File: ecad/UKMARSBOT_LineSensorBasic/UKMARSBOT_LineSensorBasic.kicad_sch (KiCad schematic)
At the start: 32 parts, among them J1 Conn_01x16, Q1 BC337, Q2 BPW85C, Q3 BPW85C, Q4 BPW85C, Q5 BPW85C, Q6 BC337

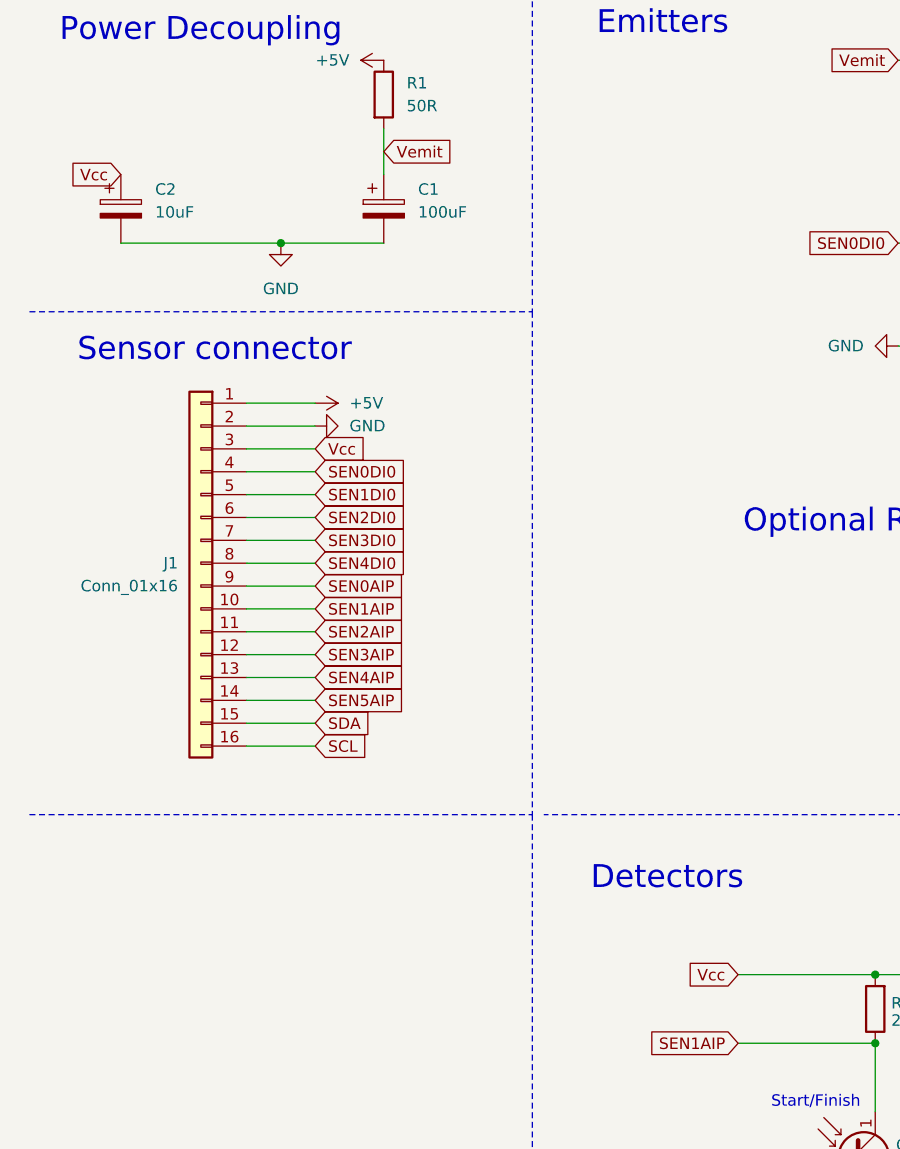
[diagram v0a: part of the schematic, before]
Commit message: Basic line sensor modified for new connector position
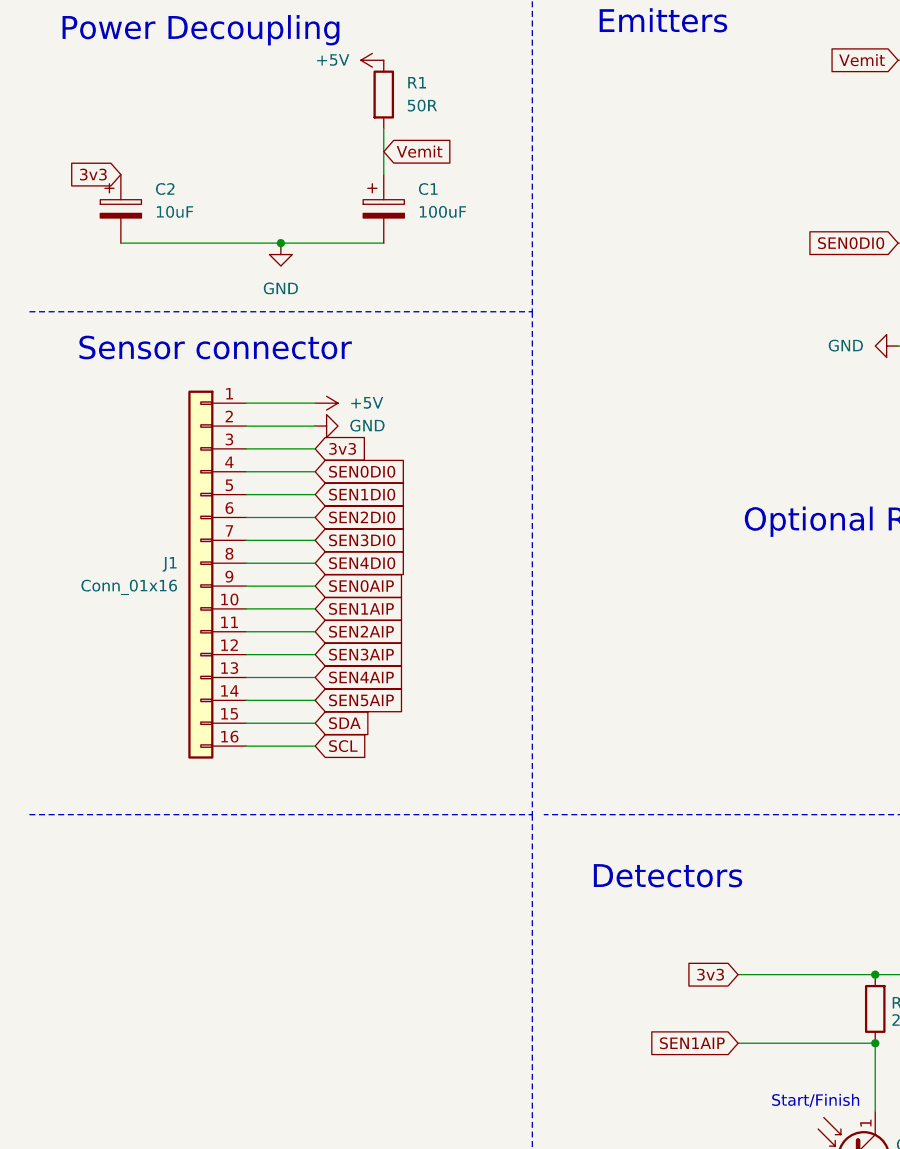
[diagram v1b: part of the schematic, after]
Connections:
- net Vcc renamed 3v3
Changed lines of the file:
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@@
 		)
 	)
-	(global_label "Vcc"
+	(global_label "3v3"
 		(shape input)
 		(at 91.44 123.19 180)
@@
 		)
 		(property "Intersheetrefs" "${INTERSHEET_REFS}"
-			(at 85.189 123.19 0)
+			(at 85.0682 123.19 0)
 			(effects
 				(font
@@
 		)
 	)
-	(global_label "Vcc"
+	(global_label "3v3"
 		(shape input)
 		(at 44.45 64.77 0)
@@
 		)
 		(property "Intersheetrefs" "${INTERSHEET_REFS}"
-			(at 50.701 64.77 0)
+			(at 50.8218 64.77 0)
 			(effects
 				(font
@@
 		)
 	)
-	(global_label "Vcc"
+	(global_label "3v3"
 		(shape input)
 		(at 22.86 34.29 180)
@@
 		)
 		(property "Intersheetrefs" "${INTERSHEET_REFS}"
-			(at 16.609 34.29 0)
+			(at 16.4882 34.29 0)
 			(effects
 				(font

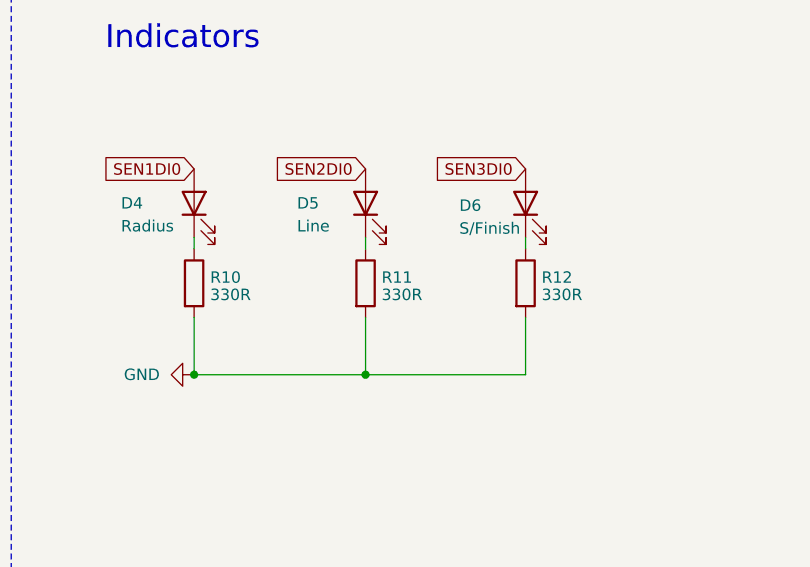
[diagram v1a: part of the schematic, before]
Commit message: Revised lime sensor board and sensor mounting hole moved forward 1.27mm for connector
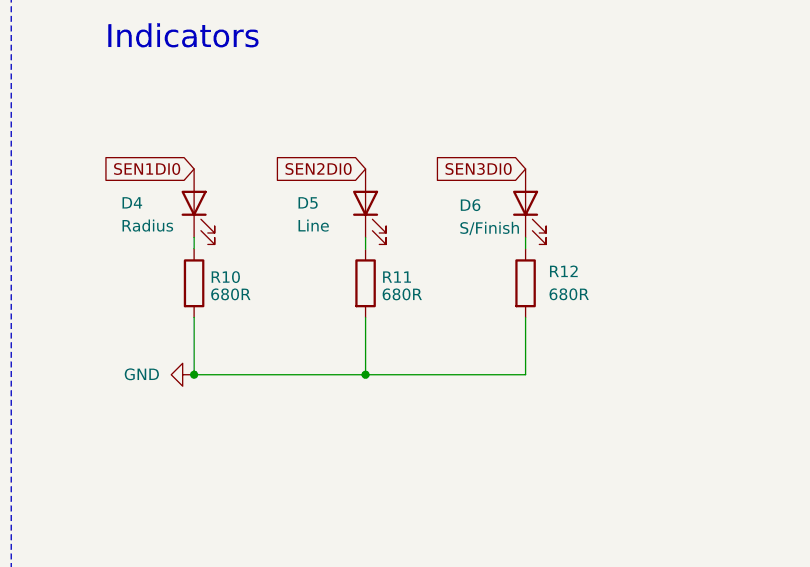
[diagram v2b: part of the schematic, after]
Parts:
- R10, R11, R12: value 330R -> 680R
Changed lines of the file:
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@@
 	(title_block
 		(title "UKMARS Gemini Line Sensor Basic")
-		(date "2025-03-04")
+		(date "2025-03-17")
 		(rev "1")
 		(company "Ian Butterworth")
@@
 			)
 		)
-		(property "Value" "330R"
+		(property "Value" "680R"
 			(at 234.188 54.6173 0)
 			(effects
@@
 		(fields_autoplaced yes)
 		(property "Reference" "R12"
-			(at 251.968 52.6963 0)
+			(at 252.73 52.0699 0)
 			(effects
 				(font
@@
 			)
 		)
-		(property "Value" "330R"
-			(at 251.968 54.6173 0)
+		(property "Value" "680R"
+			(at 252.73 54.6099 0)
 			(effects
 				(font
@@
 			)
 		)
-		(property "Value" "330R"
+		(property "Value" "680R"
 			(at 215.138 54.6173 0)
 			(effects

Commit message: Revised Wall Sensor Board consistent with hole and connector position. Fabrication files created.
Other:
- company: Ian Butterworth -> (none)
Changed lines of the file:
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@@
 		(date "2025-03-17")
 		(rev "1")
-		(company "Ian Butterworth")
 	)
 	(junction

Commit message: Reworked chassis board for production
Board reworked based on known issues from prototype builds.
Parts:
- J1: footprint Connector_PinHeader_2.54mm:PinHeader_1x16_P2.54mm_Vertical -> Connector_PinSocket_2.54mm:PinSocket_1x16_P2.54mm_Vertical
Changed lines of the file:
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@@
 			)
 		)
-		(property "Footprint" "Connector_PinHeader_2.54mm:PinHeader_1x16_P2.54mm_Vertical"
+		(property "Footprint" "Connector_PinSocket_2.54mm:PinSocket_1x16_P2.54mm_Vertical"
 			(at 31.75 77.47 0)
 			(effects

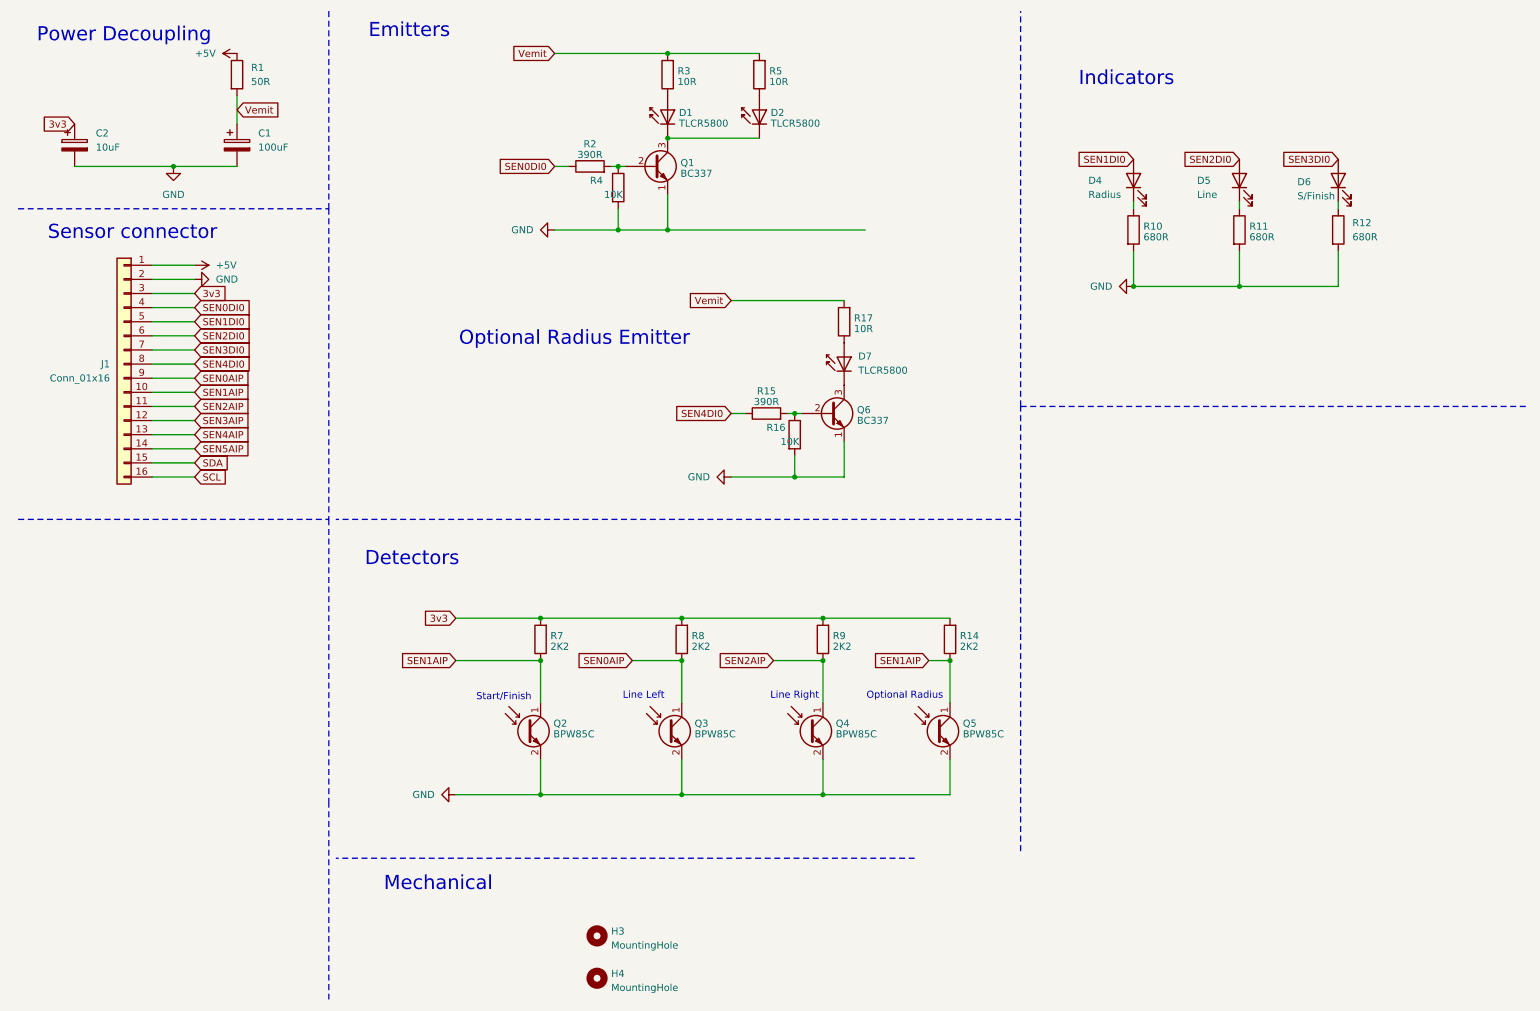
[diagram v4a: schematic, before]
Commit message: Updated basic line follower board
Updated for v2.0 board set addressing all issues raised on the prototype board.
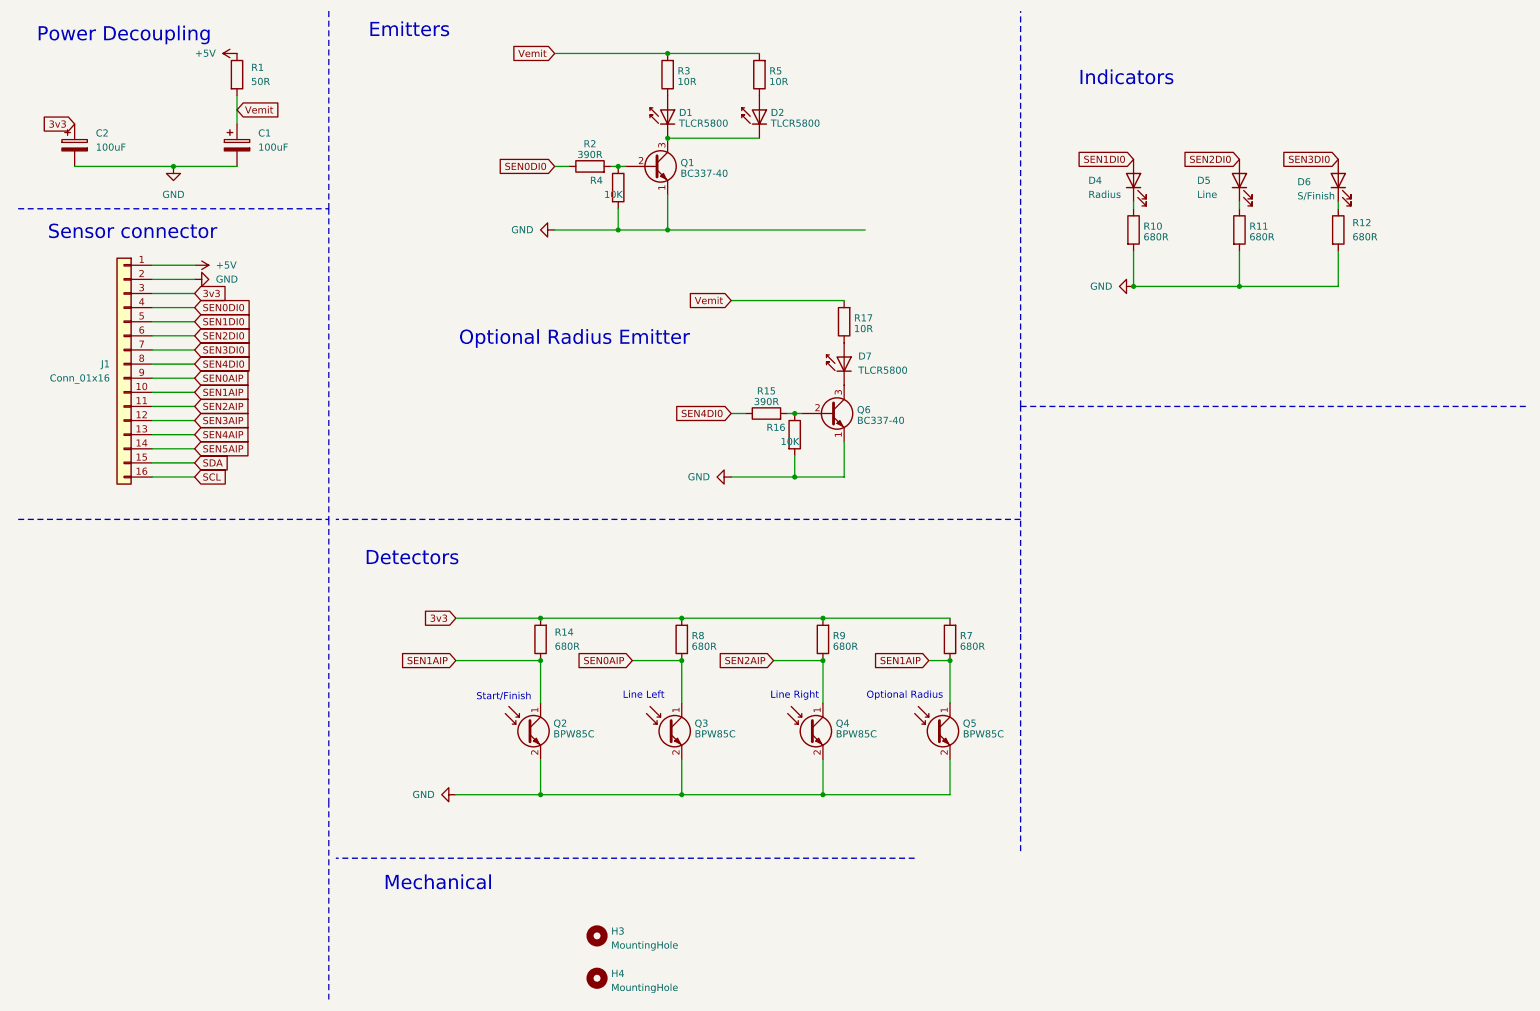
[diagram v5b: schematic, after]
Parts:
- C2: value 10uF -> 100uF
- Q1, Q6: value BC337 -> BC337-40; footprint Package_TO_SOT_THT:TO-92_HandSolder -> ukmarsbot:BC337
- R14: renamed from R7; value 2K2 -> 680R
- R7: renamed from R14; value 2K2 -> 680R
- R8, R9: value 2K2 -> 680R
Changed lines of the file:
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@@
 		(dnp no)
 		(fields_autoplaced yes)
-		(property "Reference" "R14"
+		(property "Reference" "R7"
 			(at 182.118 126.3563 0)
 			(effects
@@
 			)
 		)
-		(property "Value" "2K2"
+		(property "Value" "680R"
 			(at 182.118 128.2773 0)
 			(effects
@@
 			(project "UKMARSBOT_LineSensorBasic"
 				(path "/d8f89e6a-e7a3-4b50-a378-920a806c8e2d"
-					(reference "R14")
+					(reference "R7")
 					(unit 1)
 				)
@@
 			)
 		)
-		(property "Value" "BC337"
+		(property "Value" "BC337-40"
 			(at 131.8514 43.1873 0)
 			(effects
@@
 			)
 		)
-		(property "Footprint" "Package_TO_SOT_THT:TO-92_HandSolder"
+		(property "Footprint" "ukmarsbot:BC337"
 			(at 132.08 39.37 0)
 			(effects
@@
 			)
 		)
-		(property "Value" "2K2"
+		(property "Value" "680R"
 			(at 133.858 128.2773 0)
 			(effects
@@
 		(dnp no)
 		(fields_autoplaced yes)
-		(property "Reference" "R7"
-			(at 108.458 126.3563 0)
-			(effects
-				(font
-					(size 1.27 1.27)
-				)
-				(justify right)
-			)
-		)
-		(property "Value" "2K2"
-			(at 108.458 128.2773 0)
+		(property "Reference" "R14"
+			(at 109.22 125.7299 0)
+			(effects
+				(font
+					(size 1.27 1.27)
+				)
+				(justify right)
+			)
+		)
+		(property "Value" "680R"
+			(at 109.22 128.2699 0)
 			(effects
 				(font
@@
 			(project "UKMARSBOT_LineSensorBasic"
 				(path "/d8f89e6a-e7a3-4b50-a378-920a806c8e2d"
-					(reference "R7")
+					(reference "R14")
 					(unit 1)
 				)
@@
 			)
 		)
-		(property "Value" "2K2"
+		(property "Value" "680R"
 			(at 159.258 128.2773 0)
 			(effects
@@
 			)
 		)
-		(property "Value" "10uF"
+		(property "Value" "100uF"
 			(at 26.67 38.4809 0)
 			(effects
@@
 			)
 		)
-		(property "Value" "BC337"
+		(property "Value" "BC337-40"
 			(at 163.6014 87.6373 0)
 			(effects
@@
 			)
 		)
-		(property "Footprint" "Package_TO_SOT_THT:TO-92_HandSolder"
+		(property "Footprint" "ukmarsbot:BC337"
 			(at 163.83 83.82 0)
 			(effects

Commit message: Updated schematics to includes a new RSONLINE field and populated that field with RSOnline part numbers for most passive components
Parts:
- C1, C2: RSONLINE (none) -> 739-6799
- D1, D2, D7: RSONLINE (none) -> 818-7540
- D4, D5, D6: RSONLINE (none) -> "228-6004 or 228-5562 or 713-3974 or 813-4845"
- Q1, Q6: RSONLINE (none) -> 671-1119
- Q2, Q3, Q4, Q5: RSONLINE (none) -> 815-1263
- R10, R11, R12, R14, R7, R8, R9: RSONLINE (none) -> 707-8211
- R15, R2: RSONLINE (none) -> 707-7634
- R16, R4: RSONLINE (none) -> 707-7745
- R17, R3, R5: RSONLINE (none) -> 707-8580

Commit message: More RSONLINE part numbers and start of automated kicad exports
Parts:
- H3, H4: now left out of the parts list
- J1: Note (none) -> https://uk.rs-online.com/web/p/pcb-sockets/6816820 Need to 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; RSONLINE (none) -> 681-6820
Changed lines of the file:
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@@
 			)
 		)
-		(property "RSONLINE" ""
+		(property "RSONLINE" "681-6820"
+			(at 31.75 77.47 0)
+			(effects
+				(font
+					(size 1.27 1.27)
+				)
+				(hide yes)
+			)
+		)
+		(property "Note" "https://uk.rs-online.com/web/p/pcb-sockets/6816820 Need to be cut down"
 			(at 31.75 77.47 0)
 			(effects
@@
 		(unit 1)
 		(exclude_from_sim no)
-		(in_bom yes)
+		(in_bom no)
 		(on_board yes)
 		(dnp no)
@@
 		(unit 1)
 		(exclude_from_sim no)
-		(in_bom yes)
+		(in_bom no)
 		(on_board yes)
 		(dnp no)
